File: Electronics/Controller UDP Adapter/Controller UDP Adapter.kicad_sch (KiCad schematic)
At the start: 18 parts, among them J1 GNSS, J2 Pulse_J0011D01BNL

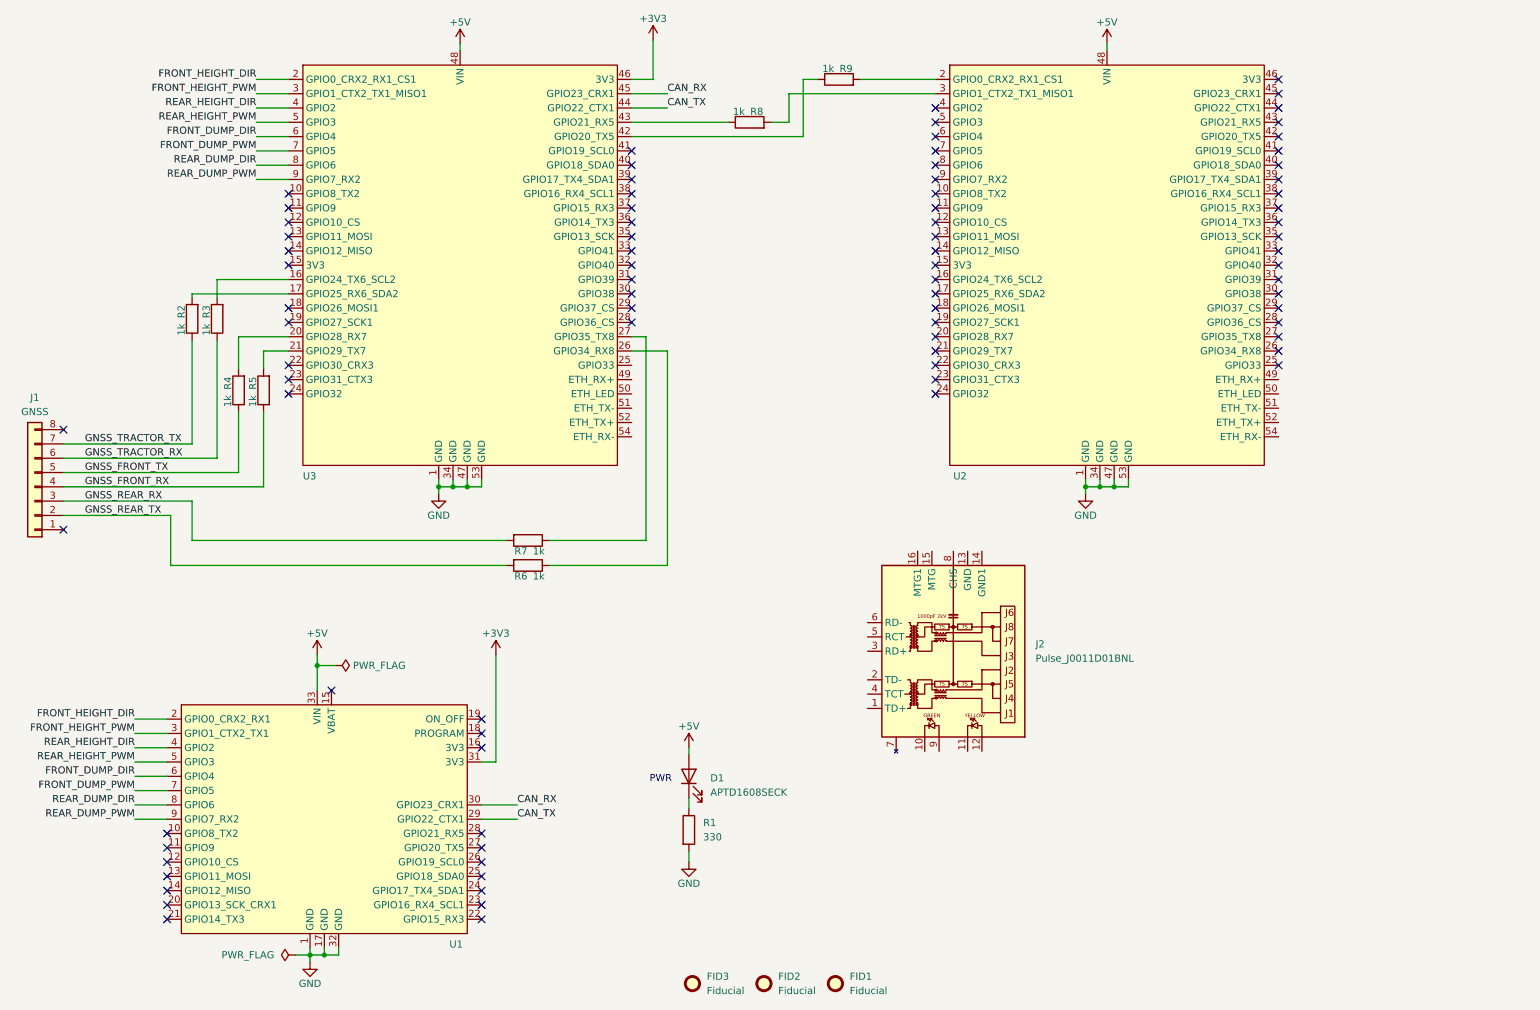
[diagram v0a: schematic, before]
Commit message: Completed V1.0 of UDP adapter.
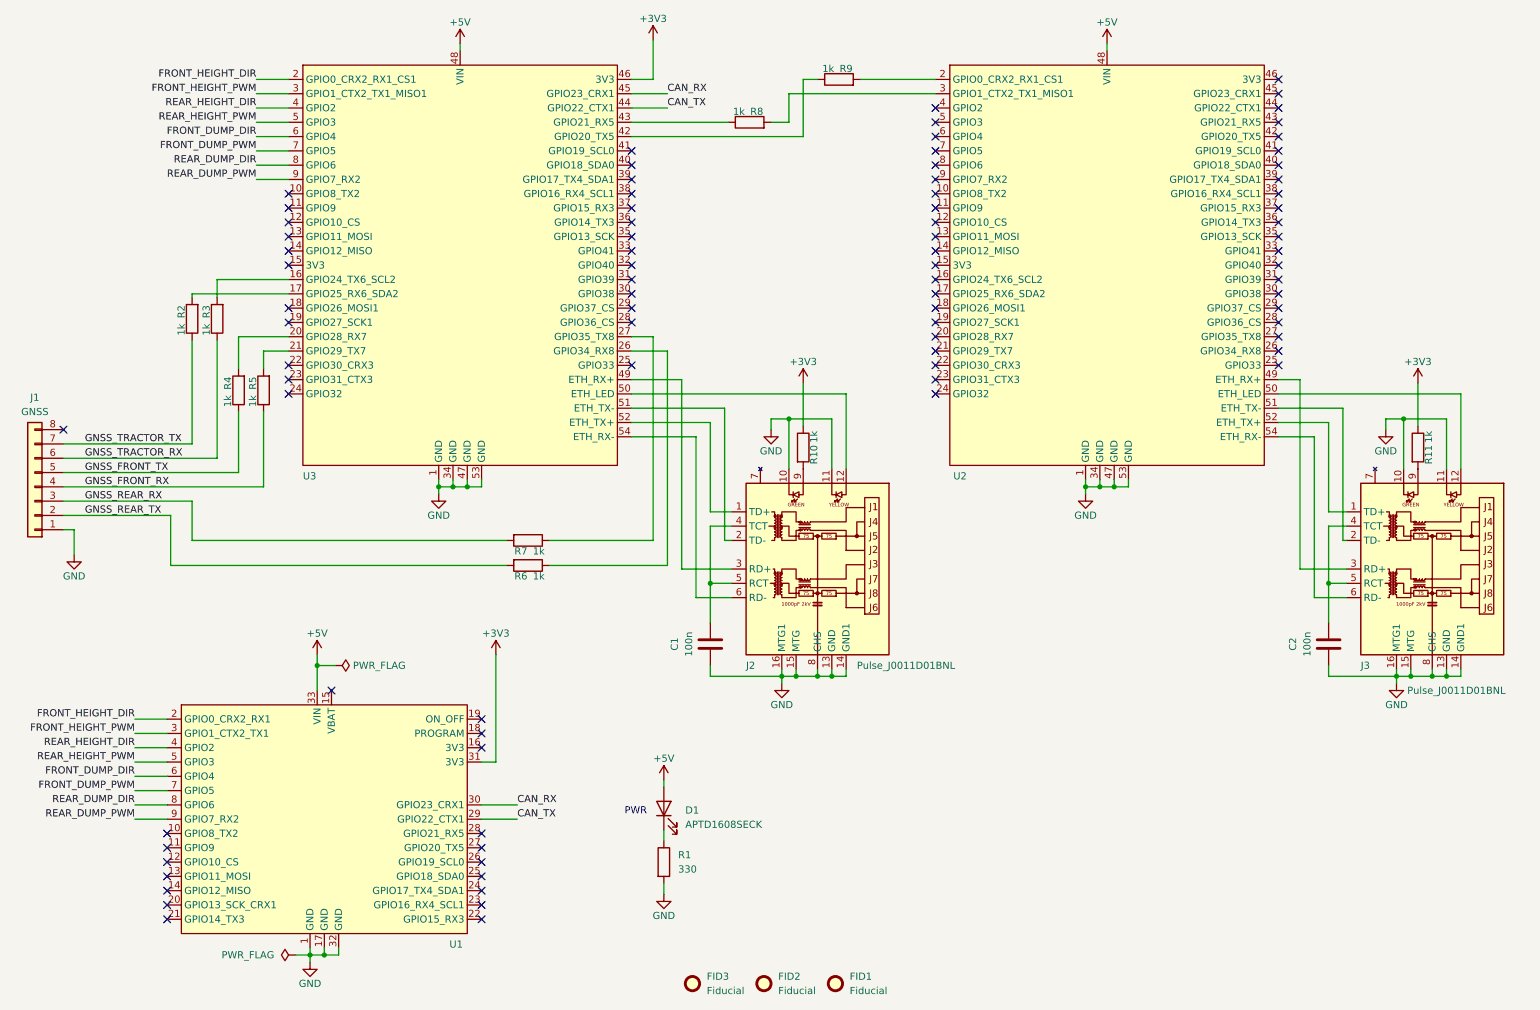
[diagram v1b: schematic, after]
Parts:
- added C1, C2: 100n, Capacitor_SMD:C_0805_2012Metric, symbol Device:C
- added J3: Pulse_J0011D01BNL, EmSA:Pulse_J0011D01BNL, symbol EmSA:Pulse_J0011D01BNL
- added R10, R11: 1k, Resistor_SMD:R_0805_2012Metric, symbol Device:R
- J2: LCSC (none) -> C581368; manf# (none) -> J0011D01BNL
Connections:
- net +3V3: now also R10.1, R11.1
- net GND: now also J1.1 (Pin_1), J2.10, J2.11, J2.13 (GND), J2.14 (GND1), J2.15 (MTG), J2.16 (MTG1), J2.8 (CHS), C1.1, C2.1, J3.10, J3.11, J3.13 (GND), J3.14 (GND1), J3.15 (MTG), J3.16 (MTG1), J3.8 (CHS)
- net at J2.1 (TD+): now also U3.52 (ETH_TX+)
- net at J2.12: now also U3.50 (ETH_LED)
- net at J2.2 (TD-): now also U3.51 (ETH_TX-)
- net at J2.3 (RD+): now also U3.49 (ETH_RX+)
- net at J2.4 (TCT): now also J2.5 (RCT), C1.2
- net at J2.6 (RD-): now also U3.54 (ETH_RX-)
- net at J2.9: now also R10.2
- net at U2.49 (ETH_RX+): now also J3.3 (RD+)
- net at U2.50 (ETH_LED): now also J3.12
- net at U2.51 (ETH_TX-): now also J3.2 (TD-)
- net at U2.52 (ETH_TX+): now also J3.1 (TD+)
- net at U2.54 (ETH_RX-): now also J3.6 (RD-)
- new net: C2.2, J3.4 (TCT), J3.5 (RCT)
- new net: J3.9, R11.2
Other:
- moved on the sheet: D1, J2, R1

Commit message: Refactor, cleanup, changed PGN value size to 64 bits. Updates to base station.
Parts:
- D1: LCSC C5879220 -> C5122084
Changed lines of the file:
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@@
       (effects (font (size 1.27 1.27)) hide)
     )
-    (property "LCSC" "C5879220" (at 132.08 161.925 0)
+    (property "LCSC" "C5122084" (at 132.08 161.925 0)
       (effects (font (size 1.27 1.27)) hide)
     )
